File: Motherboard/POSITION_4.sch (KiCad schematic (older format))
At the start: 31 parts, among them Q16 MOSFET_N_(2N7002P,215), Q17 MOSFET_N_(2N7002P,215), Q18 MOSFET_N_(FDMA430NZ), Q19 MOSFET_P_(BS250FTA)

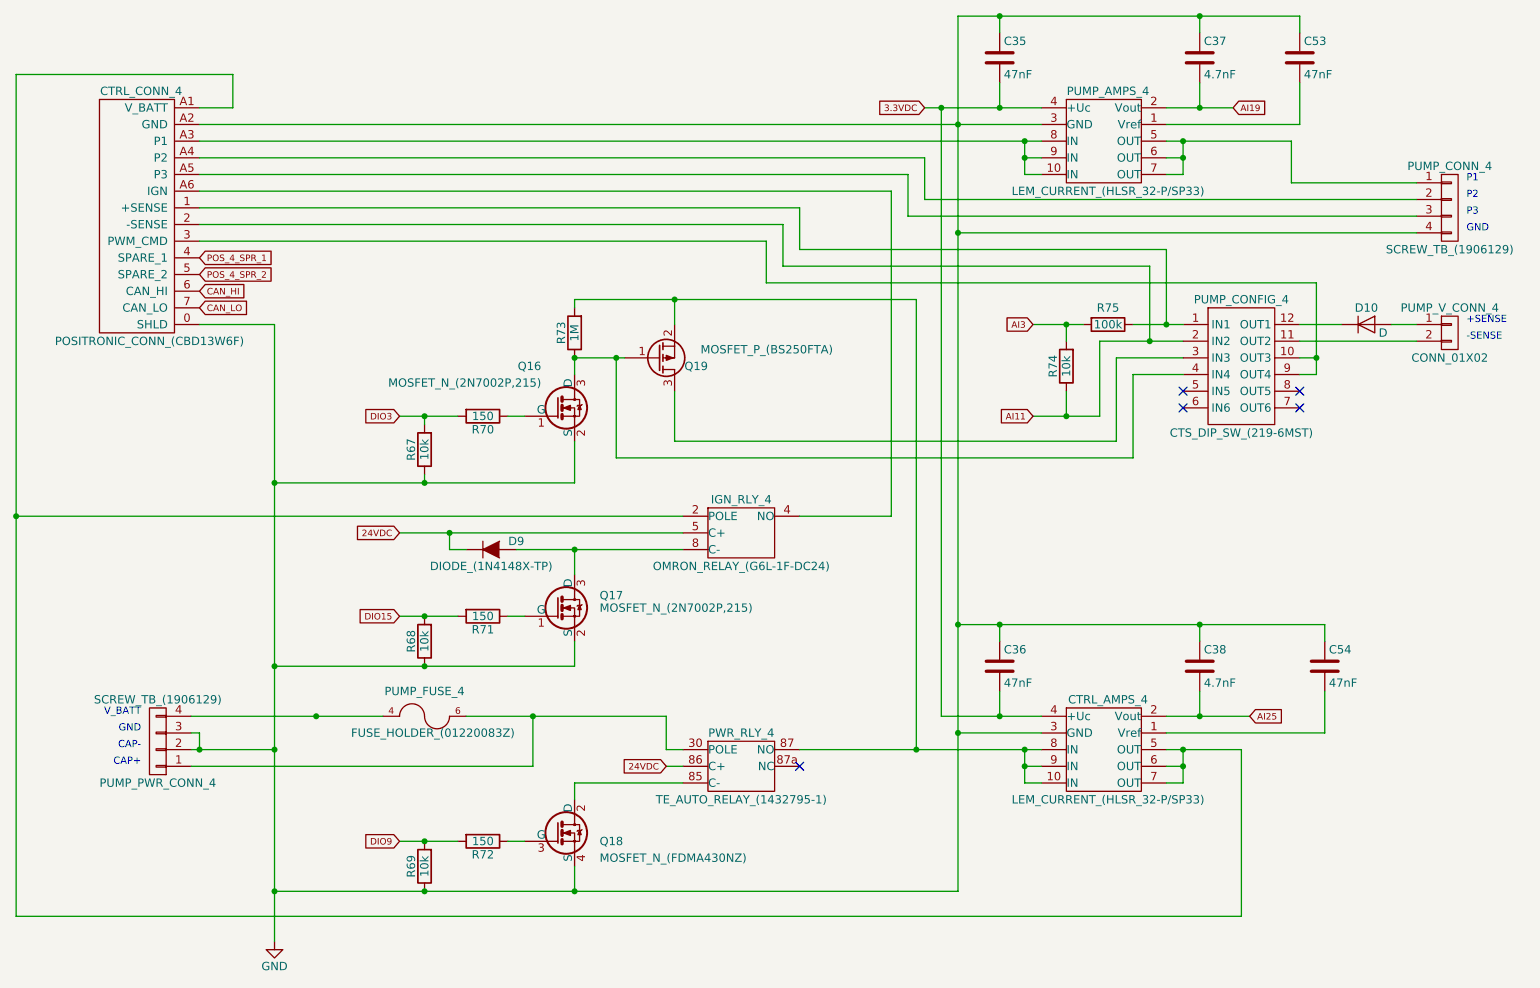
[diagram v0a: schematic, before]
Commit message: - Refer to Google Drive BOM for list of changes for v1.1 - Create drawing for Hella BLDC controller plate.
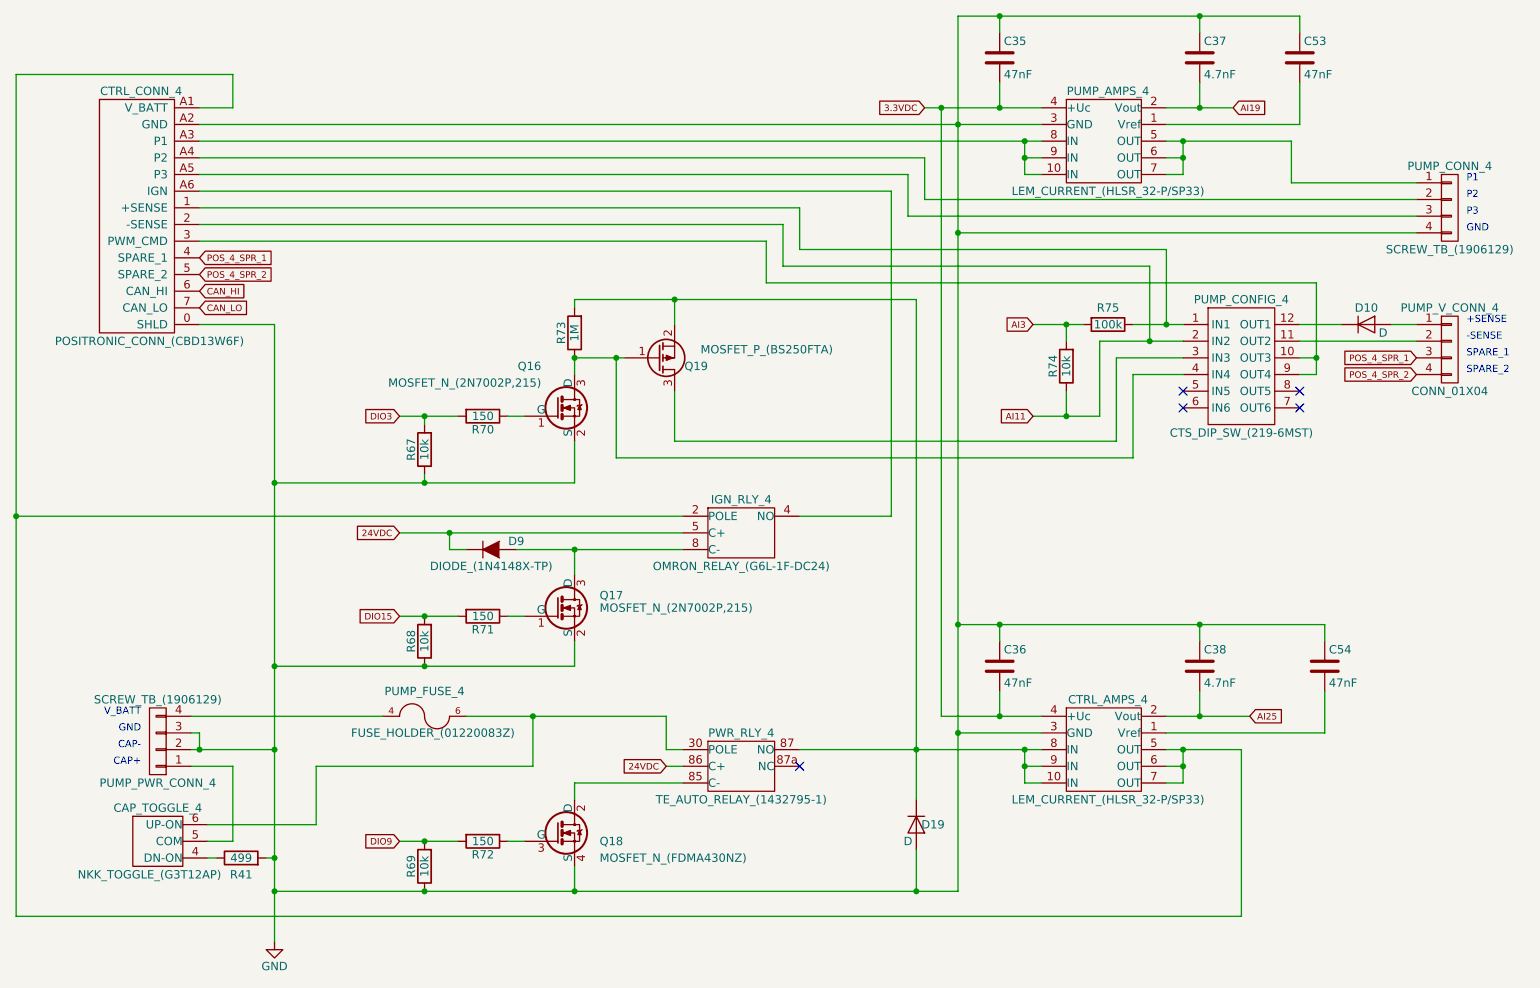
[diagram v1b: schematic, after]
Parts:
- removed PUMP_V_CONN_4: CONN_01X02, Smart_Tank:PHNX_TB_SCREW_2_POS_(1729128), symbol CONN_01X02
- added CAP_TOGGLE_4: NKK_TOGGLE_(G3T12AP), Smart_Tank:NKK_TOGGLE_(G3T12AP), symbol NKK_TOGGLE_(G3T12AP)
- added D19: D, Diodes_SMD:D_SOD-123, symbol D
- added PUMP_V_CONN_4: CONN_01X04, Smart_Tank:PHNX_TB_SCREW_4_POS_(1729144), symbol CONN_01X04
- added R41: 499, Resistors_SMD:R_1206, symbol R
- D10: footprint Diodes_SMD:SOD-523 -> Diodes_SMD:SOD-123
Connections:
- net GND: now also D19.2 (A), R41.2
- net POS_4_SPR_1: now also PUMP_V_CONN_4.3 (P3)
- net POS_4_SPR_2: now also PUMP_V_CONN_4.4 (P4)
- net at PUMP_FUSE_4.6, PUMP_FUSE_4.7, PWR_RLY_4.30 (POLE): now also CAP_TOGGLE_4.6 (UP-ON); no longer PUMP_PWR_CONN_4.1 (P1)
- net at CTRL_AMPS_4.10 (IN), CTRL_AMPS_4.8 (IN), CTRL_AMPS_4.9 (IN)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: now also D19.1 (K)
- net at PUMP_CONFIG_4.11 (OUT2): now also PUMP_V_CONN_4.2 (P2)
- net at D10.2 (A): now also PUMP_V_CONN_4.1 (P1)
- new net: CAP_TOGGLE_4.5 (COM), PUMP_PWR_CONN_4.1 (P1)
- new net: CAP_TOGGLE_4.4 (DN-ON), R41.1
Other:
- note added: "SPARE_1"
- note added: "SPARE_2"
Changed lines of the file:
@@
 CAP+
 $Comp
-L GND #PWR024
+L GND #PWR025
 U 1 1 57A9374A
 P 2950 6350
-F 0 "#PWR024" H 2950 6100 50  0001 C CNN
+F 0 "#PWR025" H 2950 6100 50  0001 C CNN
 F 1 "GND" H 2950 6200 50  0000 C CNN
 F 2 "" H 2950 6350 50  0000 C CNN
@@
 	1    0    0    -1
 $EndComp
-$Comp
-L CONN_01X02 PUMP_V_CONN_4
-U 1 1 57A93806
-P 10000 2700
-F 0 "PUMP_V_CONN_4" H 10000 2850 50  0000 C CNN
-F 1 "CONN_01X02" H 10000 2550 50  0000 C CNN
-F 2 "Smart_Tank:PHNX_TB_SCREW_2_POS_(1729128)" H 10000 2700 50  0001 C CNN
-F 3 "" H 10000 2700 50  0000 C CNN
-	1    10000 2700
-	1    0    0    -1
-$EndComp
 Text Notes 10100 2650 0    43   ~ 0
 +SENSE
@@
 	2500 5100 2500 5200
 Connection ~ 2500 5200
-Wire Wire Line
-	4500 5300 2450 5300
 Connection ~ 4500 5000
 Wire Wire Line
@@
 	4750 2500 6800 2500
 Wire Wire Line
-	6800 2500 6800 5200
+	6800 2500 6800 5500
 Connection ~ 6800 5200
 Wire Wire Line
@@
 	2950 4700 4750 4700
 Connection ~ 3850 4700
-Connection ~ 3200 5000
 Connection ~ 2950 6050
 Wire Wire Line
@@
 F 0 "D10" H 9500 2750 50  0000 C CNN
 F 1 "D" H 9600 2600 50  0000 C CNN
-F 2 "Diodes_SMD:SOD-523" H 9500 2650 50  0001 C CNN
+F 2 "Diodes_SMD:SOD-123" H 9500 2650 50  0001 C CNN
 F 3 "" H 9500 2650 50  0000 C CNN
 	1    9500 2650
@@
 	9250 4450 9250 4550
 Connection ~ 8500 4450
+$Comp
+L NKK_TOGGLE_(G3T12AP) CAP_TOGGLE_4
+U 1 1 5976B55E
+P 2250 5750
+F 0 "CAP_TOGGLE_4" H 2250 5950 50  0000 C CNN
+F 1 "NKK_TOGGLE_(G3T12AP)" H 2200 5550 50  0000 C CNN
+F 2 "Smart_Tank:NKK_TOGGLE_(G3T12AP)" H 2250 4550 50  0001 C CNN
+F 3 "" H 2250 4550 50  0000 C CNN
+	1    2250 5750
+	1    0    0    -1
+$EndComp
+Wire Wire Line
+	2450 5300 2700 5300
+Wire Wire Line
+	3200 5300 4500 5300
+$Comp
+L D D19
+U 1 1 5976C922
+P 6800 5650
+F 0 "D19" V 6800 5750 50  0000 C CNN
+F 1 "D" V 6900 5600 50  0000 C CNN
+F 2 "Diodes_SMD:D_SOD-123" H 6800 5650 50  0001 C CNN
+F 3 "" H 6800 5650 50  0000 C CNN
+	1    6800 5650
+	0    1    1    0
+$EndComp
+Wire Wire Line
+	6800 5800 6800 6050
+Connection ~ 6800 6050
+$Comp
+L R R41
+U 1 1 5978CB93
+P 2750 5850
+F 0 "R41" V 2650 5850 50  0000 C CNN
+F 1 "499" V 2750 5850 50  0000 C CNN
+F 2 "Resistors_SMD:R_1206" V 2680 5850 50  0001 C CNN
+F 3 "" H 2750 5850 50  0000 C CNN
+	1    2750 5850
+	0    -1   -1   0
+$EndComp
+Wire Wire Line
+	2550 5750 2700 5750
+Wire Wire Line
+	2700 5750 2700 5300
+Wire Wire Line
+	2550 5650 3200 5650
+Wire Wire Line
+	3200 5650 3200 5300
+Wire Wire Line
+	2550 5850 2600 5850
+Wire Wire Line
+	2900 5850 2950 5850
+Connection ~ 2950 5850
+$Comp
+L CONN_01X04 PUMP_V_CONN_4
+U 1 1 5979A2CA
+P 10000 2800
+F 0 "PUMP_V_CONN_4" H 10000 3050 50  0000 C CNN
+F 1 "CONN_01X04" H 10000 2550 50  0000 C CNN
+F 2 "Smart_Tank:PHNX_TB_SCREW_4_POS_(1729144)" H 10000 2800 50  0001 C CNN
+F 3 "" H 10000 2800 50  0001 C CNN
+	1    10000 2800
+	1    0    0    -1
+$EndComp
+Text GLabel 9800 2850 0    39   Input ~ 0
+POS_4_SPR_1
+Text GLabel 9800 2950 0    39   Input ~ 0
+POS_4_SPR_2
+Text Notes 10100 2850 0    43   ~ 0
+SPARE_1
+Text Notes 10100 2950 0    43   ~ 0
+SPARE_2
 $EndSCHEMATC

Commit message: - Created Modbus Adapter.
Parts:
- C35, C36, C37, C38, C53, C54: symbol C -> Smart-Tank-Motherboard-rescue:C
- CAP_TOGGLE_4: symbol NKK_TOGGLE_(G3T12AP) -> Smart-Tank-Motherboard-rescue:NKK_TOGGLE_(G3T12AP)
- CTRL_AMPS_4, PUMP_AMPS_4: symbol LEM_CURRENT_(HLSR_32-P/SP33) -> Smart-Tank-Motherboard-rescue:LEM_CURRENT_(HLSR_32-P_SP33)
- CTRL_CONN_4: symbol POSITRONIC_CONN_(CBD13W6F) -> Smart-Tank-Motherboard-rescue:POSITRONIC_CONN_(CBD13W6F)
- D10, D19: symbol D -> Smart-Tank-Motherboard-rescue:D
- D9: symbol DIODE_(1N4148X-TP) -> Smart-Tank-Motherboard-rescue:DIODE_(1N4148X-TP)
- IGN_RLY_4: symbol OMRON_RELAY_(G6L-1F-DC24) -> Smart-Tank-Motherboard-rescue:OMRON_RELAY_(G6L-1F-DC24)
- PUMP_CONFIG_4: symbol CTS_DIP_SW_(219-6MST) -> Smart-Tank-Motherboard-rescue:CTS_DIP_SW_(219-6MST)
- PUMP_CONN_4, PUMP_PWR_CONN_4: symbol SCREW_TB_(1906129) -> Smart-Tank-Motherboard-rescue:SCREW_TB_(1906129)
- PUMP_FUSE_4: symbol FUSE_HOLDER_(01220083Z) -> Smart-Tank-Motherboard-rescue:FUSE_HOLDER_(01220083Z)
- PUMP_V_CONN_4: symbol CONN_01X04 -> Smart-Tank-Motherboard-rescue:CONN_01X04
- PWR_RLY_4: symbol TE_AUTO_RELAY_(1432795-1) -> Smart-Tank-Motherboard-rescue:TE_AUTO_RELAY_(1432795-1)
- Q16, Q17: symbol MOSFET_N_(2N7002P,215) -> Smart-Tank-Motherboard-rescue:MOSFET_N_(2N7002P,215)
- Q18: symbol MOSFET_N_(FDMA430NZ) -> Smart-Tank-Motherboard-rescue:MOSFET_N_(FDMA430NZ)
- Q19: symbol MOSFET_P_(BS250FTA) -> Smart-Tank-Motherboard-rescue:MOSFET_P_(BS250FTA)
- R41, R67, R68, R69, R70, R71, R72, R73, R74, R75: symbol R -> Smart-Tank-Motherboard-rescue:R
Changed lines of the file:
@@
-EESchema Schematic File Version 2
-LIBS:Smart Tank Motherboard-rescue
-LIBS:power
-LIBS:device
-LIBS:transistors
-LIBS:conn
-LIBS:linear
-LIBS:regul
-LIBS:74xx
-LIBS:cmos4000
-LIBS:adc-dac
-LIBS:memory
-LIBS:xilinx
-LIBS:microcontrollers
-LIBS:dsp
-LIBS:microchip
-LIBS:analog_switches
-LIBS:motorola
-LIBS:texas
-LIBS:intel
-LIBS:audio
-LIBS:interface
-LIBS:digital-audio
-LIBS:philips
-LIBS:display
-LIBS:cypress
-LIBS:siliconi
-LIBS:opto
-LIBS:atmel
-LIBS:contrib
-LIBS:valves
+EESchema Schematic File Version 4
 LIBS:Smart Tank Motherboard-cache
-EELAYER 25 0
+EELAYER 29 0
 EELAYER END
 $Descr A4 11693 8268
@@
 $EndDescr
 $Comp
-L R R72
+L Smart-Tank-Motherboard-rescue:R R72
 U 1 1 57A93730
 P 4200 5750
@@
 $EndComp
 $Comp
-L R R69
+L Smart-Tank-Motherboard-rescue:R R69
 U 1 1 57A93737
 P 3850 5900
@@
 $EndComp
 $Comp
-L SCREW_TB_(1906129) PUMP_PWR_CONN_4
+L Smart-Tank-Motherboard-rescue:SCREW_TB_(1906129) PUMP_PWR_CONN_4
 U 1 1 57A9373F
 P 2250 5150
@@
 CAP+
 $Comp
-L GND #PWR025
+L Smart-Tank-Motherboard-rescue:GND #PWR025
 U 1 1 57A9374A
 P 2950 6350
@@
 $EndComp
 $Comp
-L SCREW_TB_(1906129) PUMP_CONN_4
+L Smart-Tank-Motherboard-rescue:SCREW_TB_(1906129) PUMP_CONN_4
 U 1 1 57A9375F
 P 10000 1950
@@
 GND
 $Comp
-L POSITRONIC_CONN_(CBD13W6F) CTRL_CONN_4
+L Smart-Tank-Motherboard-rescue:POSITRONIC_CONN_(CBD13W6F) CTRL_CONN_4
 U 1 1 57A9376A
 P 2150 1900
@@
 $EndComp
 $Comp
-L FUSE_HOLDER_(01220083Z) PUMP_FUSE_4
+L Smart-Tank-Motherboard-rescue:FUSE_HOLDER_(01220083Z) PUMP_FUSE_4
 U 1 1 57A93771
 P 3850 5000
@@
 $EndComp
 $Comp
-L MOSFET_N_(FDMA430NZ) Q18
+L Smart-Tank-Motherboard-rescue:MOSFET_N_(FDMA430NZ) Q18
 U 1 1 57A93778
 P 4650 5700
@@
 $EndComp
 $Comp
-L TE_AUTO_RELAY_(1432795-1) PWR_RLY_4
+L Smart-Tank-Motherboard-rescue:TE_AUTO_RELAY_(1432795-1) PWR_RLY_4
 U 1 1 57A9377F
 P 5650 5400
@@
 AI25
 $Comp
-L OMRON_RELAY_(G6L-1F-DC24) IGN_RLY_4
+L Smart-Tank-Motherboard-rescue:OMRON_RELAY_(G6L-1F-DC24) IGN_RLY_4
 U 1 1 57A9378B
 P 5650 4000
@@
 $EndComp
 $Comp
-L MOSFET_N_(2N7002P,215) Q17
+L Smart-Tank-Motherboard-rescue:MOSFET_N_(2N7002P,215) Q17
 U 1 1 57A93792
 P 4650 4350
@@
 $EndComp
 $Comp
-L R R71
+L Smart-Tank-Motherboard-rescue:R R71
 U 1 1 57A93799
 P 4200 4400
@@
 $EndComp
 $Comp
-L R R68
+L Smart-Tank-Motherboard-rescue:R R68
 U 1 1 57A937A0
 P 3850 4550
@@
 CAN_LO
 $Comp
-L DIODE_(1N4148X-TP) D9
+L Smart-Tank-Motherboard-rescue:DIODE_(1N4148X-TP) D9
 U 1 1 57A937AB
 P 4250 4000
@@
 POS_4_SPR_2
 $Comp
-L MOSFET_N_(2N7002P,215) Q16
+L Smart-Tank-Motherboard-rescue:MOSFET_N_(2N7002P,215) Q16
 U 1 1 57A937B4
 P 4650 3150
@@
 $EndComp
 $Comp
-L MOSFET_P_(BS250FTA) Q19
+L Smart-Tank-Motherboard-rescue:MOSFET_P_(BS250FTA) Q19
 U 1 1 57A937BB
 P 5250 2850
@@
 $EndComp
 $Comp
-L R R70
+L Smart-Tank-Motherboard-rescue:R R70
 U 1 1 57A937C2
 P 4200 3200
@@
 $EndComp
 $Comp
-L R R73
+L Smart-Tank-Motherboard-rescue:R R73
 U 1 1 57A937C9
 P 4750 2700
@@
 DIO3
 $Comp
-L R R67
+L Smart-Tank-Motherboard-rescue:R R67
 U 1 1 57A937D1
 P 3850 3400
@@
 NoConn ~ 6100 5300
 $Comp
-L C C37
+L Smart-Tank-Motherboard-rescue:C C37
 U 1 1 57A937E3
 P 8500 1050
@@
 $EndComp
 $Comp
-L C C35
+L Smart-Tank-Motherboard-rescue:C C35
 U 1 1 57A937EA
 P 7300 1050
@@
 $EndComp
 $Comp
-L C C38
+L Smart-Tank-Motherboard-rescue:C C38
 U 1 1 57A937F1
 P 8500 4700
@@
 $EndComp
 $Comp
-L C C36
+L Smart-Tank-Motherboard-rescue:C C36
 U 1 1 57A937F8
 P 7300 4700
@@
 $EndComp
 $Comp
-L CTS_DIP_SW_(219-6MST) PUMP_CONFIG_4
+L Smart-Tank-Motherboard-rescue:CTS_DIP_SW_(219-6MST) PUMP_CONFIG_4
 U 1 1 57A937FF
 P 8750 2900
@@
 NoConn ~ 8400 3150
 $Comp
-L R R74
+L Smart-Tank-Motherboard-rescue:R R74
 U 1 1 57A93813
 P 7700 2900
@@
 $EndComp
 $Comp
-L R R75
+L Smart-Tank-Motherboard-rescue:R R75
 U 1 1 57A9381A
 P 7950 2650
@@
 	4750 2550 4750 2500
 $Comp
-L D D10
+L Smart-Tank-Motherboard-rescue:D D10
 U 1 1 57A938D8
 P 9500 2650
@@
 	9650 2650 9800 2650
 $Comp
-L LEM_CURRENT_(HLSR_32-P/SP33) PUMP_AMPS_4
+L Smart-Tank-Motherboard-rescue:LEM_CURRENT_(HLSR_32-P_SP33) PUMP_AMPS_4
 U 1 1 57B7476D
 P 7800 1550
@@
 $EndComp
 $Comp
-L LEM_CURRENT_(HLSR_32-P/SP33) CTRL_AMPS_4
+L Smart-Tank-Motherboard-rescue:LEM_CURRENT_(HLSR_32-P_SP33) CTRL_AMPS_4
 U 1 1 57B76929
 P 7800 5200
@@
 Connection ~ 2950 3600
 $Comp
-L C C53
+L Smart-Tank-Motherboard-rescue:C C53
 U 1 1 57D1F6A0
 P 9100 1050
@@
 Connection ~ 8500 800
 $Comp
-L C C54
+L Smart-Tank-Motherboard-rescue:C C54
 U 1 1 57D1FD25
 P 9250 4700
@@
 Connection ~ 8500 4450
 $Comp
-L NKK_TOGGLE_(G3T12AP) CAP_TOGGLE_4
+L Smart-Tank-Motherboard-rescue:NKK_TOGGLE_(G3T12AP) CAP_TOGGLE_4
 U 1 1 5976B55E
 P 2250 5750
@@
 	3200 5300 4500 5300
 $Comp
-L D D19
+L Smart-Tank-Motherboard-rescue:D D19
 U 1 1 5976C922
 P 6800 5650
@@
 Connection ~ 6800 6050
 $Comp
-L R R41
+L Smart-Tank-Motherboard-rescue:R R41
 U 1 1 5978CB93
 P 2750 5850
@@
 Connection ~ 2950 5850
 $Comp
-L CONN_01X04 PUMP_V_CONN_4
+L Smart-Tank-Motherboard-rescue:CONN_01X04 PUMP_V_CONN_4
 U 1 1 5979A2CA
 P 10000 2800
